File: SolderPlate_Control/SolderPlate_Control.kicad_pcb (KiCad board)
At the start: 2 copper layers, 23.3 x 22 mm, 17 parts, among them J1 Encoder, Q1 Si2301CDS, Q4 Si2301CDS, U1 PEL12D

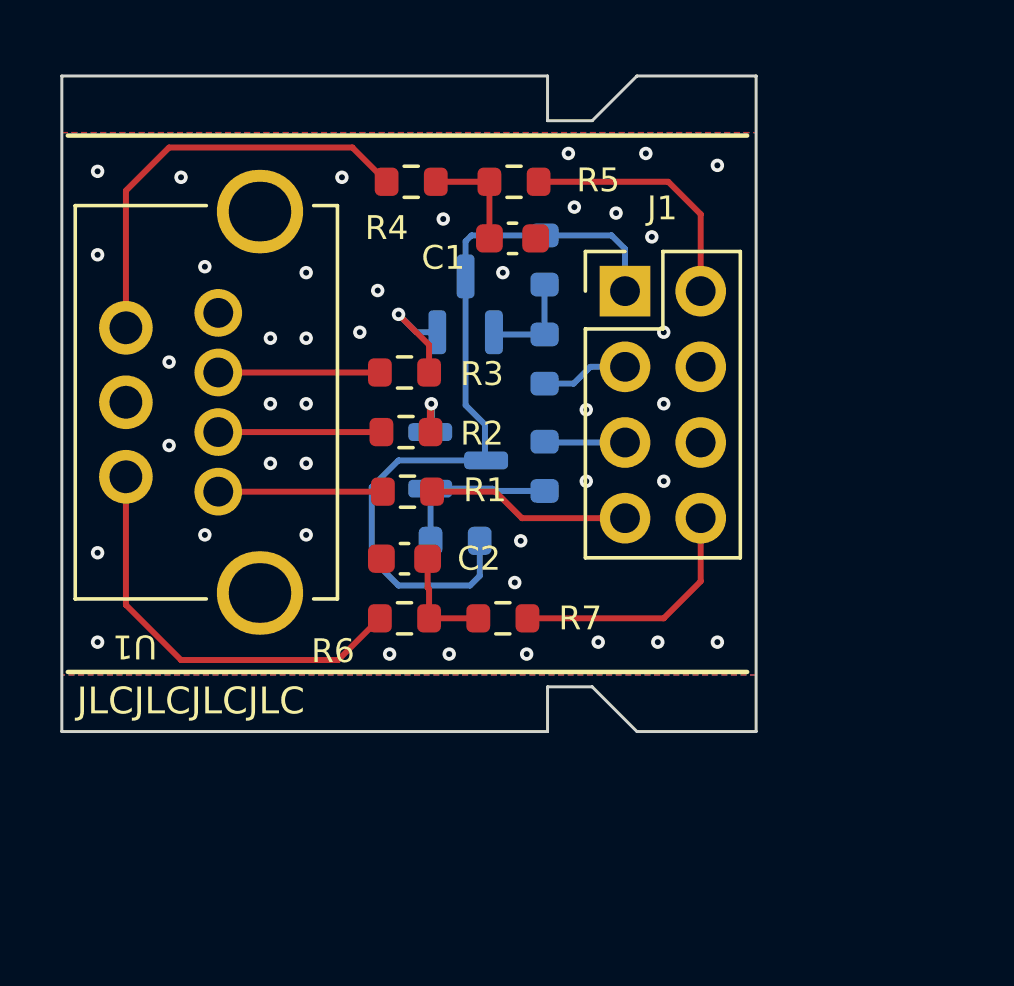
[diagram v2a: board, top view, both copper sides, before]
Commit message: Fixed wrongly routed P-MOSs in encoder control PCB
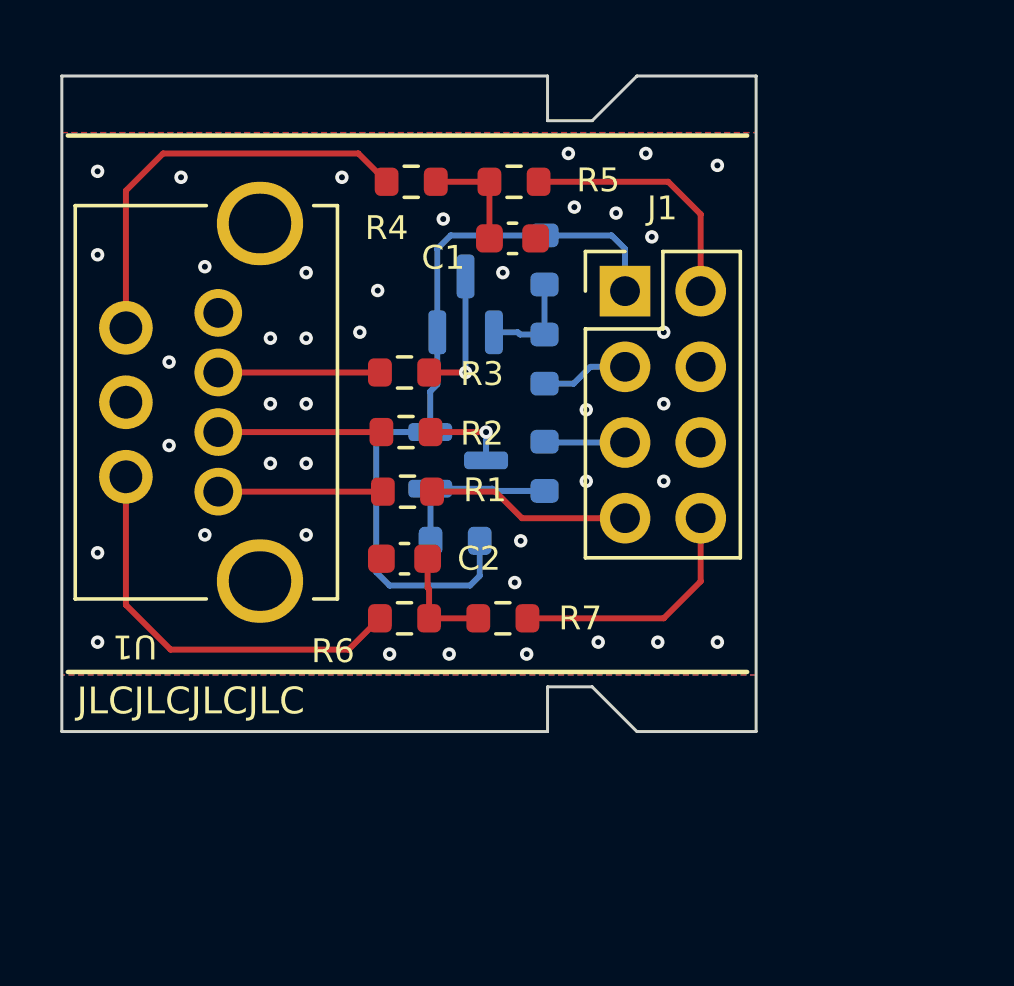
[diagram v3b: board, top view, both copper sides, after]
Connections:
- Q1 pad 2: Net-(Q1-S) -> +5V
- Q1 pad 3: +5V -> Net-(Q1-D)
- Q4 pad 2: Net-(Q4-S) -> +5V
- Q4 pad 3: +5V -> Net-(Q4-D)
- R2 pad 1: Net-(Q4-S) -> Net-(Q4-D)
- R3 pad 1: Net-(Q1-S) -> Net-(Q1-D)
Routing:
- net Net-(Q1-D): track 0.00 -> 4.45 mm, vias 0 -> 1
- net Net-(Q1-S): track 3.92 -> 0.00 mm, vias 1 -> 0
- net Net-(Q4-D): track 0.00 -> 2.81 mm, vias 0 -> 1
- net Net-(Q4-S): track 1.93 -> 0.00 mm, vias 1 -> 0
- net +5V: track 26.6 -> 25.6 mm
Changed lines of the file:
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@@
   (net 8 "/Enc_SW")
   (net 9 "/LED_Orange")
-  (net 10 "Net-(Q1-S)")
+  (net 10 "Net-(Q1-D)")
   (net 11 "Net-(Q4-G)")
   (net 12 "Net-(U1-SW)")
@@
   (net 17 "unconnected-(J1-Pin_6-Pad6)")
   (net 18 "Net-(Q1-G)")
-  (net 19 "Net-(Q4-S)")
+  (net 19 "Net-(Q4-D)")
   (footprint "Resistor_SMD:R_0603_1608Metric" (layer "F.Cu")
     (at 80.725 46.55)
@@
       (stroke (width 0.1) (type solid)) (layer "F.Fab"))
     (pad "1" smd roundrect (at -0.825 0 180) (size 0.8 0.95) (layers "F.Cu" "F.Paste" "F.Mask") (roundrect_rratio 0.25)
-      (net 19 "Net-(Q4-S)") (pintype "passive"))
+      (net 19 "Net-(Q4-D)") (pintype "passive"))
     (pad "2" smd roundrect (at 0.825 0 180) (size 0.8 0.95) (layers "F.Cu" "F.Paste" "F.Mask") (roundrect_rratio 0.25)
       (net 13 "Net-(U1-A2)") (pintype "passive"))
@@
       (stroke (width 0.1) (type solid)) (layer "F.Fab"))
     (pad "1" smd roundrect (at -0.825 0 180) (size 0.8 0.95) (layers "F.Cu" "F.Paste" "F.Mask") (roundrect_rratio 0.25)
-      (net 10 "Net-(Q1-S)") (pintype "passive"))
+      (net 10 "Net-(Q1-D)") (pintype "passive"))
     (pad "2" smd roundrect (at 0.825 0 180) (size 0.8 0.95) (layers "F.Cu" "F.Paste" "F.Mask") (roundrect_rratio 0.25)
       (net 14 "Net-(U1-A1)") (pintype "passive"))
@@
     (pad "7" thru_hole circle (at 4.5 -2.5 180) (size 1.8 1.8) (drill 1.1) (layers "*.Cu" "*.Mask")
       (net 16 "Net-(U1-B)") (pinfunction "B") (pintype "passive"))
-    (pad "SH" thru_hole oval (at 0 -6.4 180) (size 2.9 2.8) (drill oval 2.1 2) (layers "*.Cu" "*.Mask"))
-    (pad "SH" thru_hole oval (at 0 6.4 180) (size 2.9 2.8) (drill oval 2.1 2) (layers "*.Cu" "*.Mask"))
+    (pad "SH" thru_hole oval (at 0 -6 180) (size 2.9 2.8) (drill oval 2.1 2) (layers "*.Cu" "*.Mask"))
+    (pad "SH" thru_hole oval (at 0 6 180) (size 2.9 2.8) (drill oval 2.1 2) (layers "*.Cu" "*.Mask"))
   )
   (footprint "Package_TO_SOT_SMD:SOT-23" (layer "B.Cu")
@@
       (net 18 "Net-(Q1-G)") (pinfunction "G") (pintype "input"))
     (pad "2" smd roundrect (at -0.9375 -0.95 90) (size 1.475 0.6) (layers "B.Cu" "B.Paste" "B.Mask") (roundrect_rratio 0.25)
-      (net 10 "Net-(Q1-S)") (pinfunction "S") (pintype "passive"))
+      (net 5 "+5V") (pinfunction "S") (pintype "passive"))
     (pad "3" smd roundrect (at 0.9375 0 90) (size 1.475 0.6) (layers "B.Cu" "B.Paste" "B.Mask") (roundrect_rratio 0.25)
-      (net 5 "+5V") (pinfunction "D") (pintype "passive"))
+      (net 10 "Net-(Q1-D)") (pinfunction "D") (pintype "passive"))
     (model "${KICAD6_3DMODEL_DIR}/Package_TO_SOT_SMD.3dshapes/SOT-23.wrl"
       (offset (xyz 0 0 0))
@@
       (net 11 "Net-(Q4-G)") (pinfunction "G") (pintype "input"))
     (pad "2" smd roundrect (at -0.9375 -0.95) (size 1.475 0.6) (layers "B.Cu" "B.Paste" "B.Mask") (roundrect_rratio 0.25)
-      (net 19 "Net-(Q4-S)") (pinfunction "S") (pintype "passive"))
+      (net 5 "+5V") (pinfunction "S") (pintype "passive"))
     (pad "3" smd roundrect (at 0.9375 0) (size 1.475 0.6) (layers "B.Cu" "B.Paste" "B.Mask") (roundrect_rratio 0.25)
-      (net 5 "+5V") (pinfunction "D") (pintype "passive"))
+      (net 19 "Net-(Q4-D)") (pinfunction "D") (pintype "passive"))
     (model "${KICAD6_3DMODEL_DIR}/Package_TO_SOT_SMD.3dshapes/SOT-23.wrl"
       (offset (xyz 0 0 0))
@@
   (segment (start 90.44 47.64) (end 89.35 46.55) (width 0.2) (layer "F.Cu") (net 4))
   (segment (start 90.44 50.22) (end 90.44 47.64) (width 0.2) (layer "F.Cu") (net 4))
-  (segment (start 82.55 49.725) (end 82.55 54.05) (width 0.2) (layer "B.Cu") (net 5))
   (segment (start 85.2 48.35) (end 87.45 48.35) (width 0.2) (layer "B.Cu") (net 5))
-  (segment (start 79.4 59.2) (end 80.3 60.1) (width 0.2) (layer "B.Cu") (net 5))
-  (segment (start 82.55 54.05) (end 83.2 54.7) (width 0.2) (layer "B.Cu") (net 5))
-  (segment (start 82.55 48.55) (end 82.55 49.725) (width 0.2) (layer "B.Cu") (net 5))
-  (segment (start 85.2 48.35) (end 82.75 48.35) (width 0.2) (layer "B.Cu") (net 5))
-  (segment (start 79.4 56.8) (end 79.4 59.2) (width 0.2) (layer "B.Cu") (net 5))
-  (segment (start 82.7 60.1) (end 83.025 59.775) (width 0.2) (layer "B.Cu") (net 5))
-  (segment (start 80.3 60.1) (end 82.7 60.1) (width 0.2) (layer "B.Cu") (net 5))
-  (segment (start 82.75 48.35) (end 82.55 48.55) (width 0.2) (layer "B.Cu") (net 5))
+  (segment (start 83.025 58.6) (end 83.025 59.775) (width 0.2) (layer "B.Cu") (net 5))
+  (segment (start 83.025 59.775) (end 82.7 60.1) (width 0.2) (layer "B.Cu") (net 5))
+  (segment (start 79.55 55.25) (end 79.85 54.95) (width 0.2) (layer "B.Cu") (net 5))
+  (segment (start 79.85 54.95) (end 81.3625 54.95) (width 0.2) (layer "B.Cu") (net 5))
+  (segment (start 79.55 59.65) (end 79.55 55.25) (width 0.2) (layer "B.Cu") (net 5))
+  (segment (start 81.6 48.8) (end 81.6 51.6) (width 0.2) (layer "B.Cu") (net 5))
+  (segment (start 82.05 48.35) (end 81.6 48.8) (width 0.2) (layer "B.Cu") (net 5))
+  (segment (start 80 60.1) (end 79.55 59.65) (width 0.2) (layer "B.Cu") (net 5))
+  (segment (start 85.2 48.35) (end 82.05 48.35) (width 0.2) (layer "B.Cu") (net 5))
+  (segment (start 81.3625 53.5875) (end 81.3625 54.95) (width 0.2) (layer "B.Cu") (net 5))
   (segment (start 87.45 48.35) (end 87.9 48.8) (width 0.2) (layer "B.Cu") (net 5))
-  (segment (start 83.025 59.775) (end 83.025 58.6) (width 0.2) (layer "B.Cu") (net 5))
-  (segment (start 83.2375 55.9) (end 80.3 55.9) (width 0.2) (layer "B.Cu") (net 5))
-  (segment (start 83.2 54.7) (end 83.2 55.8625) (width 0.2) (layer "B.Cu") (net 5))
-  (segment (start 83.2 55.8625) (end 83.2375 55.9) (width 0.2) (layer "B.Cu") (net 5))
   (segment (start 87.9 48.8) (end 87.9 50.22) (width 0.2) (layer "B.Cu") (net 5))
-  (segment (start 80.3 55.9) (end 79.4 56.8) (width 0.2) (layer "B.Cu") (net 5))
+  (segment (start 82.7 60.1) (end 80 60.1) (width 0.2) (layer "B.Cu") (net 5))
+  (segment (start 81.6 53.35) (end 81.3625 53.5875) (width 0.2) (layer "B.Cu") (net 5))
+  (segment (start 81.6 51.6) (end 81.6 53.35) (width 0.2) (layer "B.Cu") (net 5))
   (segment (start 90.44 57.84) (end 90.44 59.96) (width 0.2) (layer "F.Cu") (net 6))
   (segment (start 90.44 59.96) (end 89.2 61.2) (width 0.2) (layer "F.Cu") (net 6))
@@
   (segment (start 87.9 55.3) (end 85.225 55.3) (width 0.2) (layer "B.Cu") (net 9))
   (segment (start 85.225 55.3) (end 85.2 55.275) (width 0.2) (layer "B.Cu") (net 9))
-  (segment (start 81.325 52.025) (end 81.325 52.95) (width 0.2) (layer "F.Cu") (net 10))
-  (segment (start 80.3 51) (end 81.325 52.025) (width 0.2) (layer "F.Cu") (net 10))
-  (via (at 80.3 51) (size 0.45) (drill 0.2) (layers "F.Cu" "B.Cu") (net 10))
-  (segment (start 81.6 51.6) (end 80.9 51.6) (width 0.2) (layer "B.Cu") (net 10))
-  (segment (start 80.9 51.6) (end 80.3 51) (width 0.2) (layer "B.Cu") (net 10))
+  (segment (start 81.325 52.95) (end 82.55 52.95) (width 0.2) (layer "F.Cu") (net 10))
+  (via (at 82.55 52.95) (size 0.45) (drill 0.2) (layers "F.Cu" "B.Cu") (net 10))
+  (segment (start 82.55 49.725) (end 82.55 52.95) (width 0.2) (layer "B.Cu") (net 10))
   (segment (start 81.375 58.6) (end 81.375 56.8625) (width 0.2) (layer "B.Cu") (net 11))
   (segment (start 83.525 56.925) (end 83.45 56.85) (width 0.2) (layer "B.Cu") (net 11))
@@
   (segment (start 79.725 54.95) (end 74.25 54.95) (width 0.2) (layer "F.Cu") (net 13))
   (segment (start 79.675 52.95) (end 74.25 52.95) (width 0.2) (layer "F.Cu") (net 14))
-  (segment (start 79.9 46.55) (end 78.75 45.4) (width 0.2) (layer "F.Cu") (net 15))
+  (segment (start 72.4 45.6) (end 71.15 46.85) (width 0.2) (layer "F.Cu") (net 15))
+  (segment (start 78.95 45.6) (end 72.4 45.6) (width 0.2) (layer "F.Cu") (net 15))
+  (segment (start 79.9 46.55) (end 78.95 45.6) (width 0.2) (layer "F.Cu") (net 15))
   (segment (start 71.15 46.85) (end 71.15 51.45) (width 0.2) (layer "F.Cu") (net 15))
-  (segment (start 72.6 45.4) (end 71.15 46.85) (width 0.2) (layer "F.Cu") (net 15))
-  (segment (start 78.75 45.4) (end 72.6 45.4) (width 0.2) (layer "F.Cu") (net 15))
-  (segment (start 78.275 62.6) (end 73 62.6) (width 0.2) (layer "F.Cu") (net 16))
+  (segment (start 79.675 61.2) (end 78.625 62.25) (width 0.2) (layer "F.Cu") (net 16))
+  (segment (start 78.625 62.25) (end 72.65 62.25) (width 0.2) (layer "F.Cu") (net 16))
+  (segment (start 72.65 62.25) (end 71.15 60.75) (width 0.2) (layer "F.Cu") (net 16))
   (segment (start 71.15 60.75) (end 71.15 56.45) (width 0.2) (layer "F.Cu") (net 16))
-  (segment (start 79.675 61.2) (end 78.275 62.6) (width 0.2) (layer "F.Cu") (net 16))
-  (segment (start 73 62.6) (end 71.15 60.75) (width 0.2) (layer "F.Cu") (net 16))
-  (segment (start 83.575 51.675) (end 83.5 51.6) (width 0.2) (layer "B.Cu") (net 18))
   (segment (start 85.2 50) (end 85.2 51.675) (width 0.2) (layer "B.Cu") (net 18))
-  (segment (start 85.2 51.675) (end 83.575 51.675) (width 0.2) (layer "B.Cu") (net 18))
-  (segment (start 81.375 54.025) (end 81.4 54) (width 0.25) (layer "F.Cu") (net 19))
-  (segment (start 81.375 54.95) (end 81.375 54.025) (width 0.25) (layer "F.Cu") (net 19))
-  (via (at 81.4 54) (size 0.45) (drill 0.2) (layers "F.Cu" "B.Cu") (net 19))
-  (segment (start 81.4 54) (end 81.4 54.9125) (width 0.25) (layer "B.Cu") (net 19))
-  (segment (start 81.4 54.9125) (end 81.3625 54.95) (width 0.25) (layer "B.Cu") (net 19))
+  (segment (start 84.375 51.675) (end 84.3 51.6) (width 0.2) (layer "B.Cu") (net 18))
+  (segment (start 85.2 51.675) (end 84.375 51.675) (width 0.2) (layer "B.Cu") (net 18))
+  (segment (start 84.3 51.6) (end 83.5 51.6) (width 0.2) (layer "B.Cu") (net 18))
+  (segment (start 83.2375 54.95) (end 81.375 54.95) (width 0.2) (layer "F.Cu") (net 19))
+  (via (at 83.2375 54.95) (size 0.45) (drill 0.2) (layers "F.Cu" "B.Cu") (net 19))
+  (segment (start 83.2375 55.9) (end 83.2375 54.95) (width 0.2) (layer "B.Cu") (net 19))
   (zone (net 2) (net_name "GND") (layers "F&B.Cu") (hatch edge 0.5)
     (connect_pads yes (clearance 0.2))
